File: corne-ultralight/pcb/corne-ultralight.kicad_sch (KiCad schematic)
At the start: 112 parts, among them J2 OLED, J7 OLED, SW1 SW_PUSH, SW10 SW_PUSH, SW11 SW_PUSH, SW12 SW_PUSH, SW13 SW_PUSH, SW14 SW_PUSH, SW15 SW_PUSH, SW16 SW_PUSH, SW17 SW_PUSH, SW18 SW_PUSH, SW19 SW_PUSH, SW2 SW_PUSH, SW20 SW_PUSH, SW21 SW_PUSH, SW22 SW_PUSH, SW23 SW_PUSH, SW24 SW_PUSH, SW25 SW_PUSH, SW26 SW_PUSH, SW27 SW_PUSH, SW28 SW_PUSH, SW29 SW_PUSH, SW3 SW_PUSH, SW30 SW_PUSH, SW31 SW_PUSH, SW32 SW_PUSH, SW33 SW_PUSH, SW34 SW_PUSH, SW35 SW_PUSH, SW36 SW_PUSH, SW37 SW_PUSH, SW38 SW_PUSH, SW39 SW_PUSH, SW4 SW_PUSH, SW40 SW_PUSH, SW41 SW_PUSH, SW42 SW_PUSH, SW5 SW_PUSH, SW6 SW_PUSH, SW7 SW_PUSH, SW8 SW_PUSH, SW9 SW_PUSH, U1 ProMicro, U2 ProMicro

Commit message: No choc to improve clearance
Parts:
- SW1, SW10, SW11, SW12, SW13, SW14, SW15, SW16, SW17, SW18, SW19, SW2, SW20, SW22, SW23, SW24, SW25, SW26, SW27, SW28, SW29, SW3, SW30, SW31, SW32, SW33, SW34, SW35, SW36, SW37, SW38, SW39, SW4, SW40, SW41, SW5, SW6, SW7, SW8, SW9: footprint gateron-ks27:gateron-ks27-choc-v1-mx -> gateron-ks27:gateron-ks27-mx
- SW21, SW42: footprint gateron-ks27:gateron-ks27-choc-v1-mx-1.5u -> gateron-ks27:gateron-ks27-mx-1.5u
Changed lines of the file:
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@@
 			)
 		)
-		(property "Footprint" "gateron-ks27:gateron-ks27-choc-v1-mx"
+		(property "Footprint" "gateron-ks27:gateron-ks27-mx"
 			(at 41.275 24.13 0)
 			(effects
@@
 			)
 		)
-		(property "Footprint" "gateron-ks27:gateron-ks27-choc-v1-mx"
+		(property "Footprint" "gateron-ks27:gateron-ks27-mx"
 			(at 59.055 24.13 0)
 			(effects
@@
 			)
 		)
-		(property "Footprint" "gateron-ks27:gateron-ks27-choc-v1-mx"
+		(property "Footprint" "gateron-ks27:gateron-ks27-mx"
 			(at 76.835 24.13 0)
 			(effects
@@
 			)
 		)
-		(property "Footprint" "gateron-ks27:gateron-ks27-choc-v1-mx"
+		(property "Footprint" "gateron-ks27:gateron-ks27-mx"
 			(at 94.615 24.13 0)
 			(effects
@@
 			)
 		)
-		(property "Footprint" "gateron-ks27:gateron-ks27-choc-v1-mx"
+		(property "Footprint" "gateron-ks27:gateron-ks27-mx"
 			(at 112.395 24.13 0)
 			(effects
@@
 			)
 		)
-		(property "Footprint" "gateron-ks27:gateron-ks27-choc-v1-mx"
+		(property "Footprint" "gateron-ks27:gateron-ks27-mx"
 			(at 23.495 24.13 0)
 			(effects
@@
 			)
 		)
-		(property "Footprint" "gateron-ks27:gateron-ks27-choc-v1-mx"
+		(property "Footprint" "gateron-ks27:gateron-ks27-mx"
 			(at 41.275 39.37 0)
 			(effects
@@
 			)
 		)
-		(property "Footprint" "gateron-ks27:gateron-ks27-choc-v1-mx"
+		(property "Footprint" "gateron-ks27:gateron-ks27-mx"
 			(at 59.055 39.37 0)
 			(effects
@@
 			)
 		)
-		(property "Footprint" "gateron-ks27:gateron-ks27-choc-v1-mx"
+		(property "Footprint" "gateron-ks27:gateron-ks27-mx"
 			(at 76.835 39.37 0)
 			(effects
@@
 			)
 		)
-		(property "Footprint" "gateron-ks27:gateron-ks27-choc-v1-mx"
+		(property "Footprint" "gateron-ks27:gateron-ks27-mx"
 			(at 94.615 39.37 0)
 			(effects
@@
 			)
 		)
-		(property "Footprint" "gateron-ks27:gateron-ks27-choc-v1-mx"
+		(property "Footprint" "gateron-ks27:gateron-ks27-mx"
 			(at 112.395 39.37 0)
 			(effects
@@
 			)
 		)
-		(property "Footprint" "gateron-ks27:gateron-ks27-choc-v1-mx"
+		(property "Footprint" "gateron-ks27:gateron-ks27-mx"
 			(at 23.495 39.37 0)
 			(effects
@@
 			)
 		)
-		(property "Footprint" "gateron-ks27:gateron-ks27-choc-v1-mx"
+		(property "Footprint" "gateron-ks27:gateron-ks27-mx"
 			(at 41.275 54.61 0)
 			(effects
@@
 			)
 		)
-		(property "Footprint" "gateron-ks27:gateron-ks27-choc-v1-mx"
+		(property "Footprint" "gateron-ks27:gateron-ks27-mx"
 			(at 59.055 54.61 0)
 			(effects
@@
 			)
 		)
-		(property "Footprint" "gateron-ks27:gateron-ks27-choc-v1-mx"
+		(property "Footprint" "gateron-ks27:gateron-ks27-mx"
 			(at 76.835 54.61 0)
 			(effects
@@
 			)
 		)
-		(property "Footprint" "gateron-ks27:gateron-ks27-choc-v1-mx"
+		(property "Footprint" "gateron-ks27:gateron-ks27-mx"
 			(at 94.615 54.61 0)
 			(effects
@@
 			)
 		)
-		(property "Footprint" "gateron-ks27:gateron-ks27-choc-v1-mx"
+		(property "Footprint" "gateron-ks27:gateron-ks27-mx"
 			(at 112.395 54.61 0)
 			(effects
@@
 			)
 		)
-		(property "Footprint" "gateron-ks27:gateron-ks27-choc-v1-mx"
+		(property "Footprint" "gateron-ks27:gateron-ks27-mx"
 			(at 23.495 54.61 0)
 			(effects
@@
 			)
 		)
-		(property "Footprint" "gateron-ks27:gateron-ks27-choc-v1-mx"
+		(property "Footprint" "gateron-ks27:gateron-ks27-mx"
 			(at 94.615 69.85 0)
 			(effects
@@
 			)
 		)
-		(property "Footprint" "gateron-ks27:gateron-ks27-choc-v1-mx-1.5u"
+		(property "Footprint" "gateron-ks27:gateron-ks27-mx-1.5u"
 			(at 112.395 69.85 0)
 			(effects
@@
 			)
 		)
-		(property "Footprint" "gateron-ks27:gateron-ks27-choc-v1-mx"
+		(property "Footprint" "gateron-ks27:gateron-ks27-mx"
 			(at 76.835 69.85 0)
 			(effects
@@
 			)
 		)
-		(property "Footprint" "gateron-ks27:gateron-ks27-choc-v1-mx"
+		(property "Footprint" "gateron-ks27:gateron-ks27-mx"
 			(at 41.91 106.68 0)
 			(effects
@@
 			)
 		)
-		(property "Footprint" "gateron-ks27:gateron-ks27-choc-v1-mx"
+		(property "Footprint" "gateron-ks27:gateron-ks27-mx"
 			(at 59.69 106.68 0)
 			(effects
@@
 			)
 		)
-		(property "Footprint" "gateron-ks27:gateron-ks27-choc-v1-mx"
+		(property "Footprint" "gateron-ks27:gateron-ks27-mx"
 			(at 77.47 106.68 0)
 			(effects
@@
 			)
 		)
-		(property "Footprint" "gateron-ks27:gateron-ks27-choc-v1-mx"
+		(property "Footprint" "gateron-ks27:gateron-ks27-mx"
 			(at 95.25 106.68 0)
 			(effects
@@
 			)
 		)
-		(property "Footprint" "gateron-ks27:gateron-ks27-choc-v1-mx"
+		(property "Footprint" "gateron-ks27:gateron-ks27-mx"
 			(at 113.03 106.68 0)
 			(effects
@@
 			)
 		)
-		(property "Footprint" "gateron-ks27:gateron-ks27-choc-v1-mx"
+		(property "Footprint" "gateron-ks27:gateron-ks27-mx"
 			(at 24.13 106.68 0)
 			(effects
@@
 			)
 		)
-		(property "Footprint" "gateron-ks27:gateron-ks27-choc-v1-mx"
+		(property "Footprint" "gateron-ks27:gateron-ks27-mx"
 			(at 41.91 121.92 0)
 			(effects
@@
 			)
 		)
-		(property "Footprint" "gateron-ks27:gateron-ks27-choc-v1-mx"
+		(property "Footprint" "gateron-ks27:gateron-ks27-mx"
 			(at 59.69 121.92 0)
 			(effects
@@
 			)
 		)
-		(property "Footprint" "gateron-ks27:gateron-ks27-choc-v1-mx"
+		(property "Footprint" "gateron-ks27:gateron-ks27-mx"
 			(at 77.47 121.92 0)
 			(effects
@@
 			)
 		)
-		(property "Footprint" "gateron-ks27:gateron-ks27-choc-v1-mx"
+		(property "Footprint" "gateron-ks27:gateron-ks27-mx"
 			(at 95.25 121.92 0)
 			(effects
@@
 			)
 		)
-		(property "Footprint" "gateron-ks27:gateron-ks27-choc-v1-mx"
+		(property "Footprint" "gateron-ks27:gateron-ks27-mx"
 			(at 113.03 121.92 0)
 			(effects
@@
 			)
 		)
-		(property "Footprint" "gateron-ks27:gateron-ks27-choc-v1-mx"
+		(property "Footprint" "gateron-ks27:gateron-ks27-mx"
 			(at 24.13 121.92 0)
 			(effects
@@
 			)
 		)
-		(property "Footprint" "gateron-ks27:gateron-ks27-choc-v1-mx"
+		(property "Footprint" "gateron-ks27:gateron-ks27-mx"
 			(at 41.91 137.16 0)
 			(effects
@@
 			)
 		)
-		(property "Footprint" "gateron-ks27:gateron-ks27-choc-v1-mx"
+		(property "Footprint" "gateron-ks27:gateron-ks27-mx"
 			(at 59.69 137.16 0)
 			(effects
@@
 			)
 		)
-		(property "Footprint" "gateron-ks27:gateron-ks27-choc-v1-mx"
+		(property "Footprint" "gateron-ks27:gateron-ks27-mx"
 			(at 77.47 137.16 0)
 			(effects
@@
 			)
 		)
-		(property "Footprint" "gateron-ks27:gateron-ks27-choc-v1-mx"
+		(property "Footprint" "gateron-ks27:gateron-ks27-mx"
 			(at 95.25 137.16 0)
 			(effects
@@
 			)
 		)
-		(property "Footprint" "gateron-ks27:gateron-ks27-choc-v1-mx"
+		(property "Footprint" "gateron-ks27:gateron-ks27-mx"
 			(at 113.03 137.16 0)
 			(effects
@@
 			)
 		)
-		(property "Footprint" "gateron-ks27:gateron-ks27-choc-v1-mx"
+		(property "Footprint" "gateron-ks27:gateron-ks27-mx"
 			(at 24.13 137.16 0)
 			(effects
@@
 			)
 		)
-		(property "Footprint" "gateron-ks27:gateron-ks27-choc-v1-mx"
+		(property "Footprint" "gateron-ks27:gateron-ks27-mx"
 			(at 95.25 152.4 0)
 			(effects
@@
 			)
 		)
-		(property "Footprint" "gateron-ks27:gateron-ks27-choc-v1-mx-1.5u"
+		(property "Footprint" "gateron-ks27:gateron-ks27-mx-1.5u"
 			(at 113.03 152.4 0)
 			(effects
@@
 			)
 		)
-		(property "Footprint" "gateron-ks27:gateron-ks27-choc-v1-mx"
+		(property "Footprint" "gateron-ks27:gateron-ks27-mx"
 			(at 77.47 152.4 0)
 			(effects

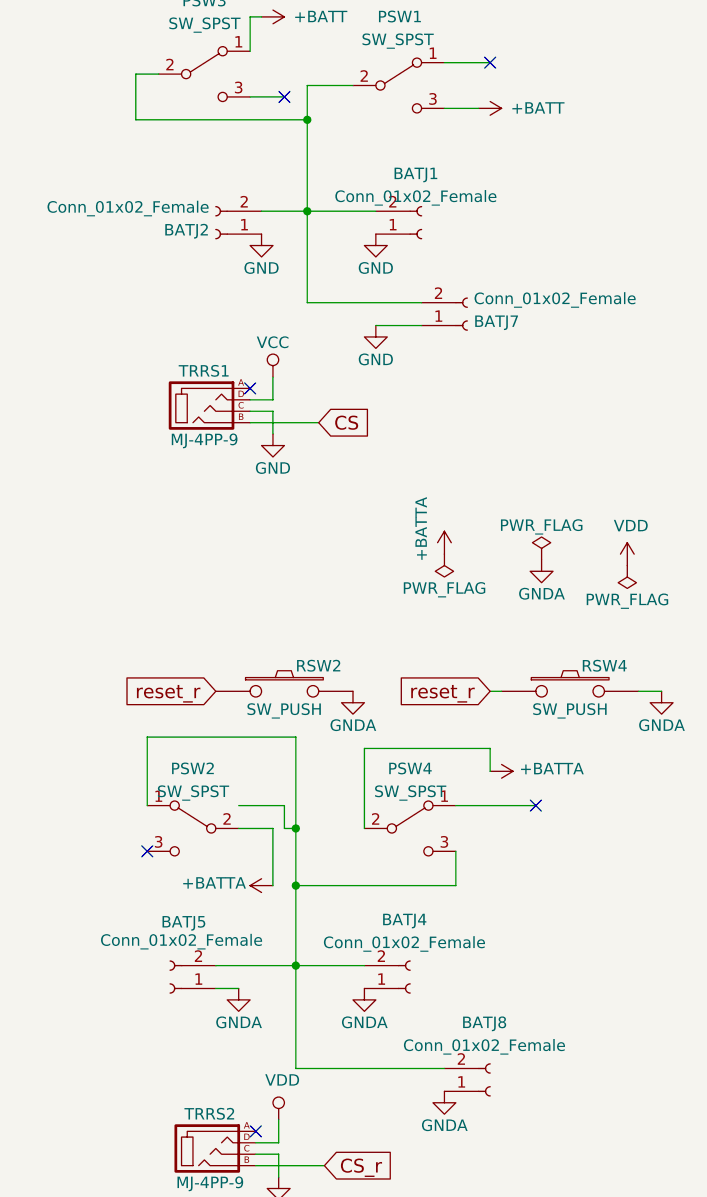
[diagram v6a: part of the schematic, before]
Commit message: One batt connector less
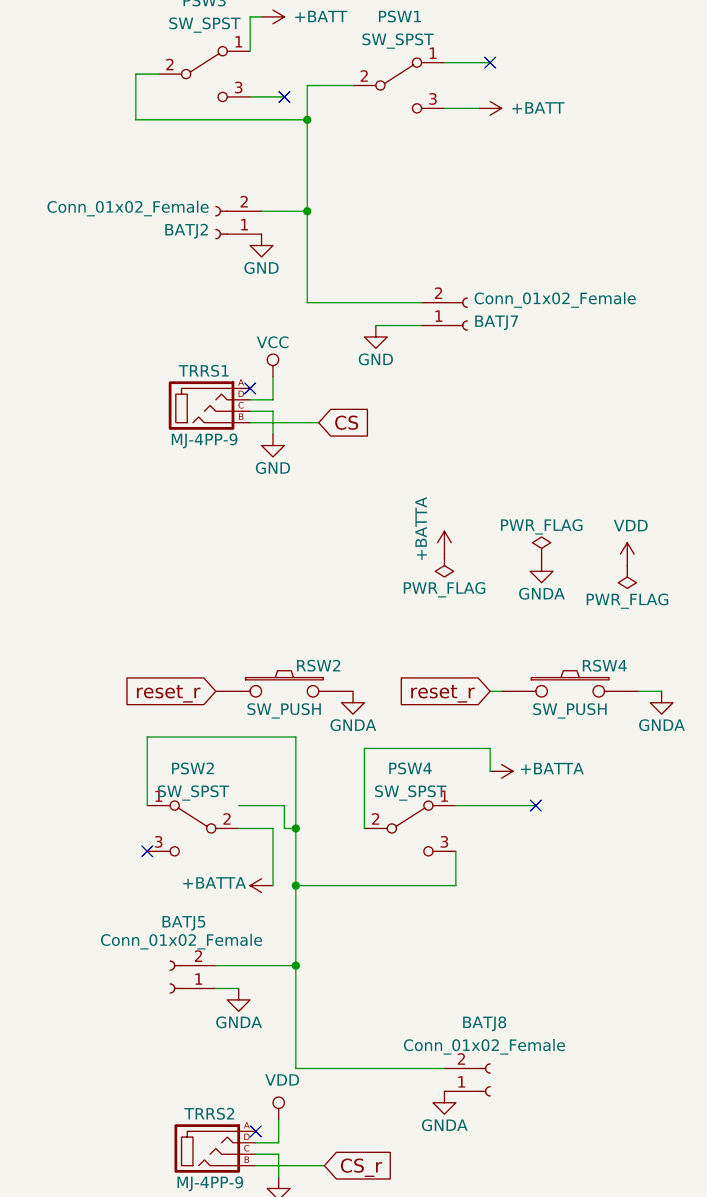
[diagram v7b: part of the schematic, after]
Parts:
- removed BATJ1, BATJ4: Conn_01x02_Female, Connector_JST:JST_PH_S2B-PH-K_1x02_P2.00mm_Horizontal, symbol Connector:Conn_01x02_Female

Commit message: chocs are back, rerouting to allow removing the hole contact
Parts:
- SW1, SW10, SW11, SW12, SW13, SW14, SW15, SW16, SW17, SW18, SW19, SW2, SW20, SW22, SW23, SW24, SW25, SW26, SW27, SW28, SW29, SW3, SW30, SW31, SW32, SW33, SW34, SW35, SW36, SW37, SW38, SW39, SW4, SW40, SW41, SW5, SW6, SW7, SW8, SW9: footprint gateron-ks27:gateron-ks27-mx -> gateron-ks27:gateron-ks27-choc-v1-mx
- SW21, SW42: footprint gateron-ks27:gateron-ks27-mx-1.5u -> gateron-ks27:gateron-ks27-choc-v1-mx-1.5u
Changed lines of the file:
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@@
 			)
 		)
-		(property "Footprint" "gateron-ks27:gateron-ks27-mx"
+		(property "Footprint" "gateron-ks27:gateron-ks27-choc-v1-mx"
 			(at 41.275 24.13 0)
 			(effects
@@
 			)
 		)
-		(property "Footprint" "gateron-ks27:gateron-ks27-mx"
+		(property "Footprint" "gateron-ks27:gateron-ks27-choc-v1-mx"
 			(at 59.055 24.13 0)
 			(effects
@@
 			)
 		)
-		(property "Footprint" "gateron-ks27:gateron-ks27-mx"
+		(property "Footprint" "gateron-ks27:gateron-ks27-choc-v1-mx"
 			(at 76.835 24.13 0)
 			(effects
@@
 			)
 		)
-		(property "Footprint" "gateron-ks27:gateron-ks27-mx"
+		(property "Footprint" "gateron-ks27:gateron-ks27-choc-v1-mx"
 			(at 94.615 24.13 0)
 			(effects
@@
 			)
 		)
-		(property "Footprint" "gateron-ks27:gateron-ks27-mx"
+		(property "Footprint" "gateron-ks27:gateron-ks27-choc-v1-mx"
 			(at 112.395 24.13 0)
 			(effects
@@
 			)
 		)
-		(property "Footprint" "gateron-ks27:gateron-ks27-mx"
+		(property "Footprint" "gateron-ks27:gateron-ks27-choc-v1-mx"
 			(at 23.495 24.13 0)
 			(effects
@@
 			)
 		)
-		(property "Footprint" "gateron-ks27:gateron-ks27-mx"
+		(property "Footprint" "gateron-ks27:gateron-ks27-choc-v1-mx"
 			(at 41.275 39.37 0)
 			(effects
@@
 			)
 		)
-		(property "Footprint" "gateron-ks27:gateron-ks27-mx"
+		(property "Footprint" "gateron-ks27:gateron-ks27-choc-v1-mx"
 			(at 59.055 39.37 0)
 			(effects
@@
 			)
 		)
-		(property "Footprint" "gateron-ks27:gateron-ks27-mx"
+		(property "Footprint" "gateron-ks27:gateron-ks27-choc-v1-mx"
 			(at 76.835 39.37 0)
 			(effects
@@
 			)
 		)
-		(property "Footprint" "gateron-ks27:gateron-ks27-mx"
+		(property "Footprint" "gateron-ks27:gateron-ks27-choc-v1-mx"
 			(at 94.615 39.37 0)
 			(effects
@@
 			)
 		)
-		(property "Footprint" "gateron-ks27:gateron-ks27-mx"
+		(property "Footprint" "gateron-ks27:gateron-ks27-choc-v1-mx"
 			(at 112.395 39.37 0)
 			(effects
@@
 			)
 		)
-		(property "Footprint" "gateron-ks27:gateron-ks27-mx"
+		(property "Footprint" "gateron-ks27:gateron-ks27-choc-v1-mx"
 			(at 23.495 39.37 0)
 			(effects
@@
 			)
 		)
-		(property "Footprint" "gateron-ks27:gateron-ks27-mx"
+		(property "Footprint" "gateron-ks27:gateron-ks27-choc-v1-mx"
 			(at 41.275 54.61 0)
 			(effects
@@
 			)
 		)
-		(property "Footprint" "gateron-ks27:gateron-ks27-mx"
+		(property "Footprint" "gateron-ks27:gateron-ks27-choc-v1-mx"
 			(at 59.055 54.61 0)
 			(effects
@@
 			)
 		)
-		(property "Footprint" "gateron-ks27:gateron-ks27-mx"
+		(property "Footprint" "gateron-ks27:gateron-ks27-choc-v1-mx"
 			(at 76.835 54.61 0)
 			(effects
@@
 			)
 		)
-		(property "Footprint" "gateron-ks27:gateron-ks27-mx"
+		(property "Footprint" "gateron-ks27:gateron-ks27-choc-v1-mx"
 			(at 94.615 54.61 0)
 			(effects
@@
 			)
 		)
-		(property "Footprint" "gateron-ks27:gateron-ks27-mx"
+		(property "Footprint" "gateron-ks27:gateron-ks27-choc-v1-mx"
 			(at 112.395 54.61 0)
 			(effects
@@
 			)
 		)
-		(property "Footprint" "gateron-ks27:gateron-ks27-mx"
+		(property "Footprint" "gateron-ks27:gateron-ks27-choc-v1-mx"
 			(at 23.495 54.61 0)
 			(effects
@@
 			)
 		)
-		(property "Footprint" "gateron-ks27:gateron-ks27-mx"
+		(property "Footprint" "gateron-ks27:gateron-ks27-choc-v1-mx"
 			(at 94.615 69.85 0)
 			(effects
@@
 			)
 		)
-		(property "Footprint" "gateron-ks27:gateron-ks27-mx-1.5u"
+		(property "Footprint" "gateron-ks27:gateron-ks27-choc-v1-mx-1.5u"
 			(at 112.395 69.85 0)
 			(effects
@@
 			)
 		)
-		(property "Footprint" "gateron-ks27:gateron-ks27-mx"
+		(property "Footprint" "gateron-ks27:gateron-ks27-choc-v1-mx"
 			(at 76.835 69.85 0)
 			(effects
@@
 			)
 		)
-		(property "Footprint" "gateron-ks27:gateron-ks27-mx"
+		(property "Footprint" "gateron-ks27:gateron-ks27-choc-v1-mx"
 			(at 41.91 106.68 0)
 			(effects
@@
 			)
 		)
-		(property "Footprint" "gateron-ks27:gateron-ks27-mx"
+		(property "Footprint" "gateron-ks27:gateron-ks27-choc-v1-mx"
 			(at 59.69 106.68 0)
 			(effects
@@
 			)
 		)
-		(property "Footprint" "gateron-ks27:gateron-ks27-mx"
+		(property "Footprint" "gateron-ks27:gateron-ks27-choc-v1-mx"
 			(at 77.47 106.68 0)
 			(effects
@@
 			)
 		)
-		(property "Footprint" "gateron-ks27:gateron-ks27-mx"
+		(property "Footprint" "gateron-ks27:gateron-ks27-choc-v1-mx"
 			(at 95.25 106.68 0)
 			(effects
@@
 			)
 		)
-		(property "Footprint" "gateron-ks27:gateron-ks27-mx"
+		(property "Footprint" "gateron-ks27:gateron-ks27-choc-v1-mx"
 			(at 113.03 106.68 0)
 			(effects
@@
 			)
 		)
-		(property "Footprint" "gateron-ks27:gateron-ks27-mx"
+		(property "Footprint" "gateron-ks27:gateron-ks27-choc-v1-mx"
 			(at 24.13 106.68 0)
 			(effects
@@
 			)
 		)
-		(property "Footprint" "gateron-ks27:gateron-ks27-mx"
+		(property "Footprint" "gateron-ks27:gateron-ks27-choc-v1-mx"
 			(at 41.91 121.92 0)
 			(effects
@@
 			)
 		)
-		(property "Footprint" "gateron-ks27:gateron-ks27-mx"
+		(property "Footprint" "gateron-ks27:gateron-ks27-choc-v1-mx"
 			(at 59.69 121.92 0)
 			(effects
@@
 			)
 		)
-		(property "Footprint" "gateron-ks27:gateron-ks27-mx"
+		(property "Footprint" "gateron-ks27:gateron-ks27-choc-v1-mx"
 			(at 77.47 121.92 0)
 			(effects
@@
 			)
 		)
-		(property "Footprint" "gateron-ks27:gateron-ks27-mx"
+		(property "Footprint" "gateron-ks27:gateron-ks27-choc-v1-mx"
 			(at 95.25 121.92 0)
 			(effects
@@
 			)
 		)
-		(property "Footprint" "gateron-ks27:gateron-ks27-mx"
+		(property "Footprint" "gateron-ks27:gateron-ks27-choc-v1-mx"
 			(at 113.03 121.92 0)
 			(effects
@@
 			)
 		)
-		(property "Footprint" "gateron-ks27:gateron-ks27-mx"
+		(property "Footprint" "gateron-ks27:gateron-ks27-choc-v1-mx"
 			(at 24.13 121.92 0)
 			(effects
@@
 			)
 		)
-		(property "Footprint" "gateron-ks27:gateron-ks27-mx"
+		(property "Footprint" "gateron-ks27:gateron-ks27-choc-v1-mx"
 			(at 41.91 137.16 0)
 			(effects
@@
 			)
 		)
-		(property "Footprint" "gateron-ks27:gateron-ks27-mx"
+		(property "Footprint" "gateron-ks27:gateron-ks27-choc-v1-mx"
 			(at 59.69 137.16 0)
 			(effects
@@
 			)
 		)
-		(property "Footprint" "gateron-ks27:gateron-ks27-mx"
+		(property "Footprint" "gateron-ks27:gateron-ks27-choc-v1-mx"
 			(at 77.47 137.16 0)
 			(effects
@@
 			)
 		)
-		(property "Footprint" "gateron-ks27:gateron-ks27-mx"
+		(property "Footprint" "gateron-ks27:gateron-ks27-choc-v1-mx"
 			(at 95.25 137.16 0)
 			(effects
@@
 			)
 		)
-		(property "Footprint" "gateron-ks27:gateron-ks27-mx"
+		(property "Footprint" "gateron-ks27:gateron-ks27-choc-v1-mx"
 			(at 113.03 137.16 0)
 			(effects
@@
 			)
 		)
-		(property "Footprint" "gateron-ks27:gateron-ks27-mx"
+		(property "Footprint" "gateron-ks27:gateron-ks27-choc-v1-mx"
 			(at 24.13 137.16 0)
 			(effects
@@
 			)
 		)
-		(property "Footprint" "gateron-ks27:gateron-ks27-mx"
+		(property "Footprint" "gateron-ks27:gateron-ks27-choc-v1-mx"
 			(at 95.25 152.4 0)
 			(effects
@@
 			)
 		)
-		(property "Footprint" "gateron-ks27:gateron-ks27-mx-1.5u"
+		(property "Footprint" "gateron-ks27:gateron-ks27-choc-v1-mx-1.5u"
 			(at 113.03 152.4 0)
 			(effects
@@
 			)
 		)
-		(property "Footprint" "gateron-ks27:gateron-ks27-mx"
+		(property "Footprint" "gateron-ks27:gateron-ks27-choc-v1-mx"
 			(at 77.47 152.4 0)
 			(effects
